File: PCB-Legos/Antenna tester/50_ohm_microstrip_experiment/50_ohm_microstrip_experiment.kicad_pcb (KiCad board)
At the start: 4 copper layers, 45.7 x 66.5 mm, 9 parts, among them J1 Conn_Coaxial, J3 Conn_Coaxial, J4 Conn_Coaxial, J5 Conn_Coaxial

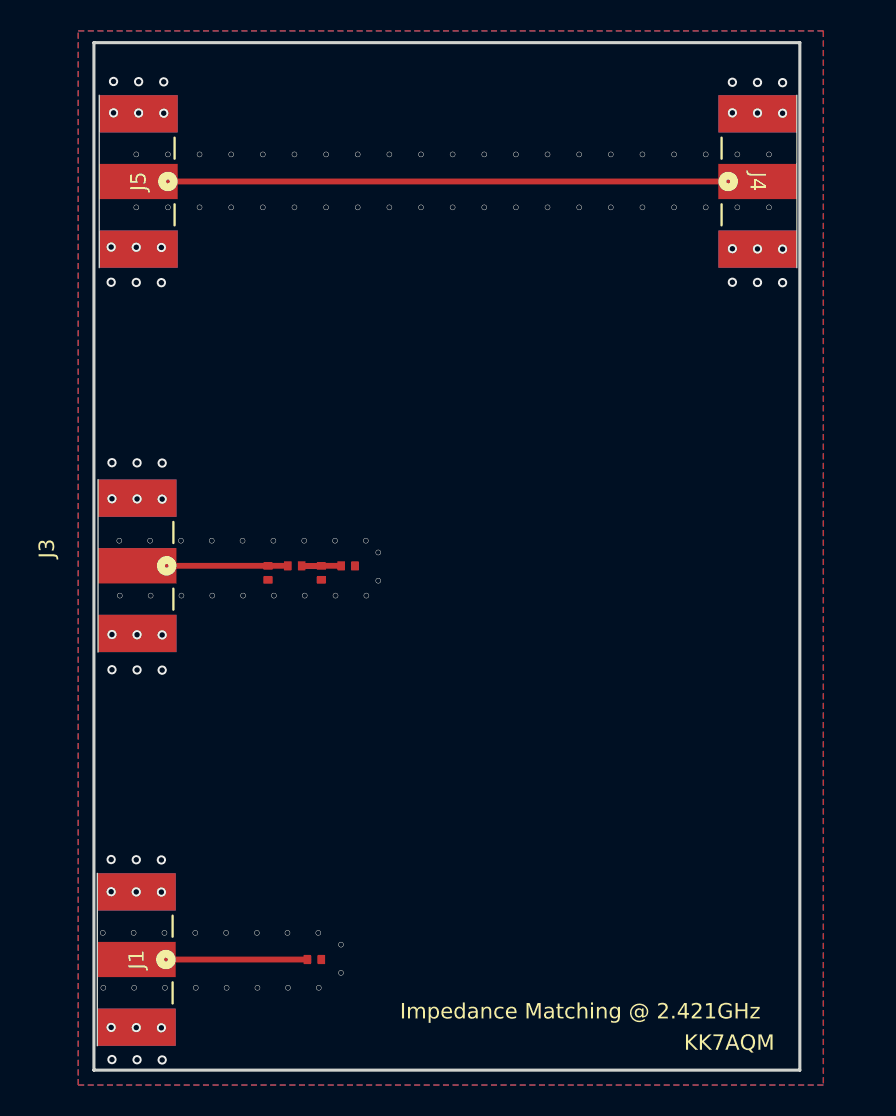
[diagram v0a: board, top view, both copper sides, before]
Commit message: Update with open stub/ changes
-Added vias, removed DNP components, moved components closer together
- implemented open stub experiment
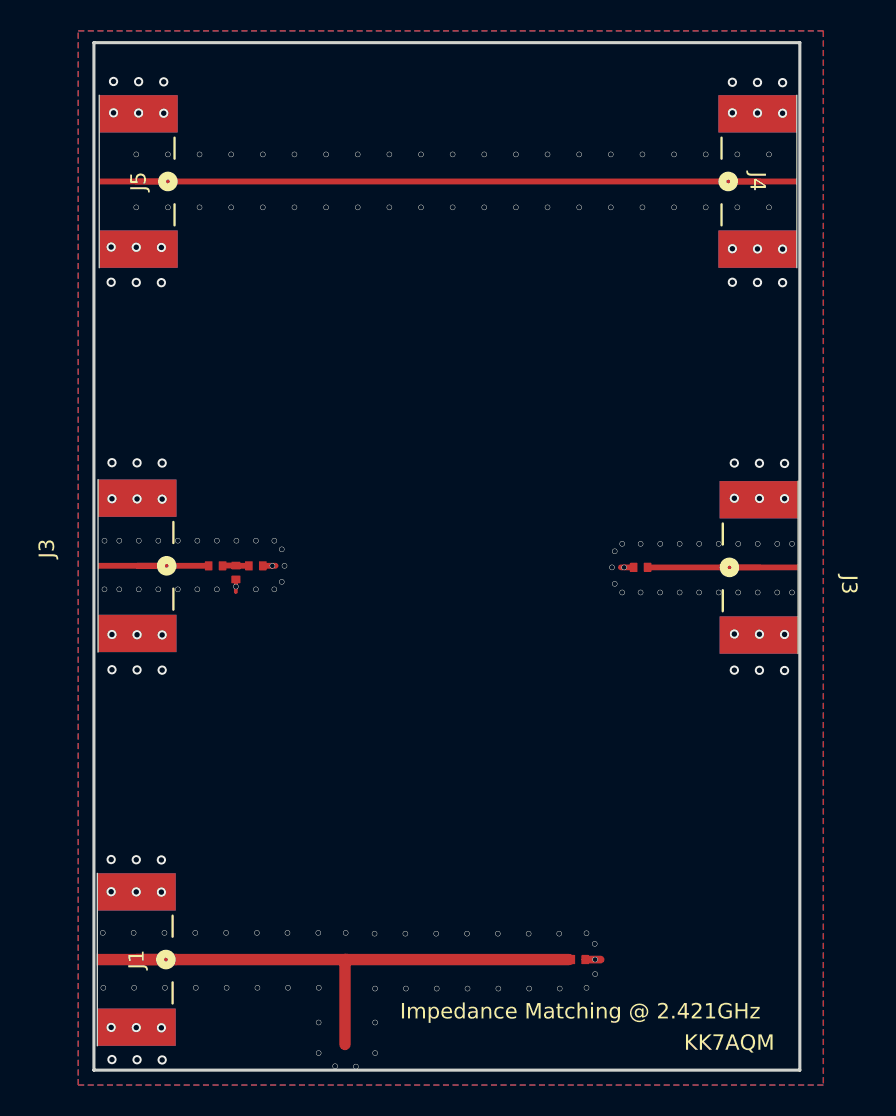
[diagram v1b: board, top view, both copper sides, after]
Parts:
- removed R4: 0, HGS_Reflector:.0402-C-NOSILK
- added J3: Conn_Coaxial, Cinch:CONN_142-0701-851_CIN, F.Cu at (174.3, 64.2)
- added R5: 0, HGS_Reflector:.0402-C-NOSILK, F.Cu at (166.5, 64.2)
- R1: value 50 -> 150
- moved R1 17.1 mm to (162.4, 89.6)
- moved R5 5.97 mm to (141.6, 64.1)
- moved R2 5.54 mm to (140.3, 64.5)
- moved R3 5.12 mm to (138.9, 64.1)
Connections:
- J1 pad 4: GND -> (no net)
- J1 pad 5: GND -> (no net)
- J3 pad 4: GND -> (no net)
- J3 pad 5: GND -> (no net)
- J4 pad 4: GND -> (no net)
- J4 pad 5: GND -> (no net)
- J5 pad 4: GND -> (no net)
- J5 pad 5: GND -> (no net)
- R1 pad 1: GND -> Net-(J1-Pad1)
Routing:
- net Net-(J1-Pad1): track 11.3 -> 34.7 mm
- net GND: track 0.00 -> 2.53 mm, vias 128 -> 192
- net Net-(J3-Pad1): track 9.75 -> 11.9 mm
- net Net-(R2-Pad2): track 2.63 -> 1.82 mm

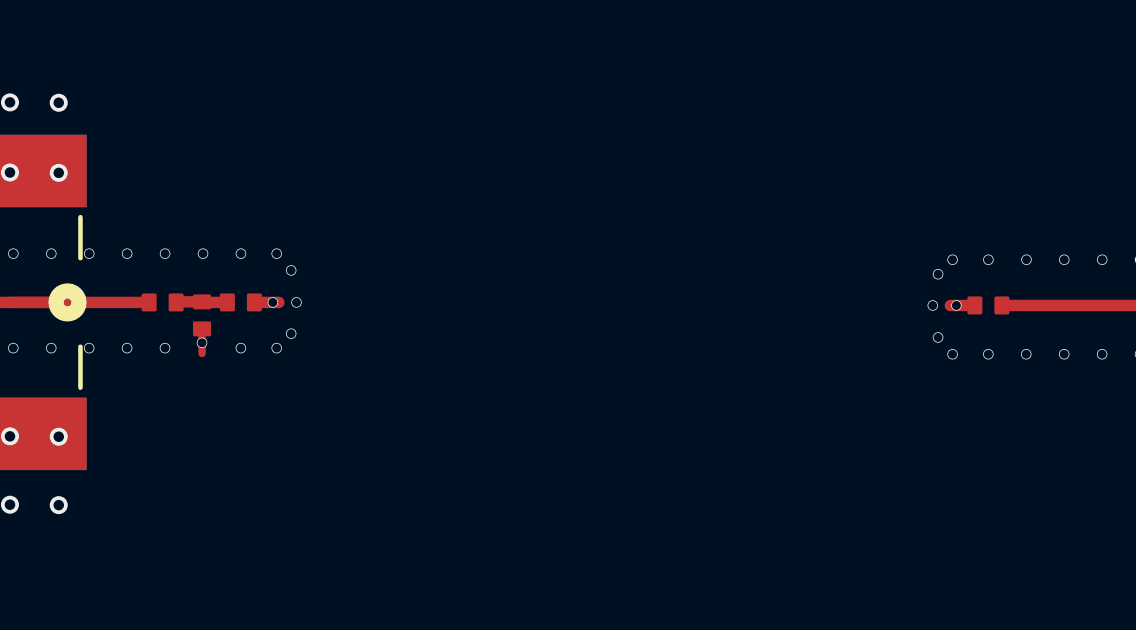
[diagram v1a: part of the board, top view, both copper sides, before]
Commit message: Matching Board with open stub
Added extra vias around pads
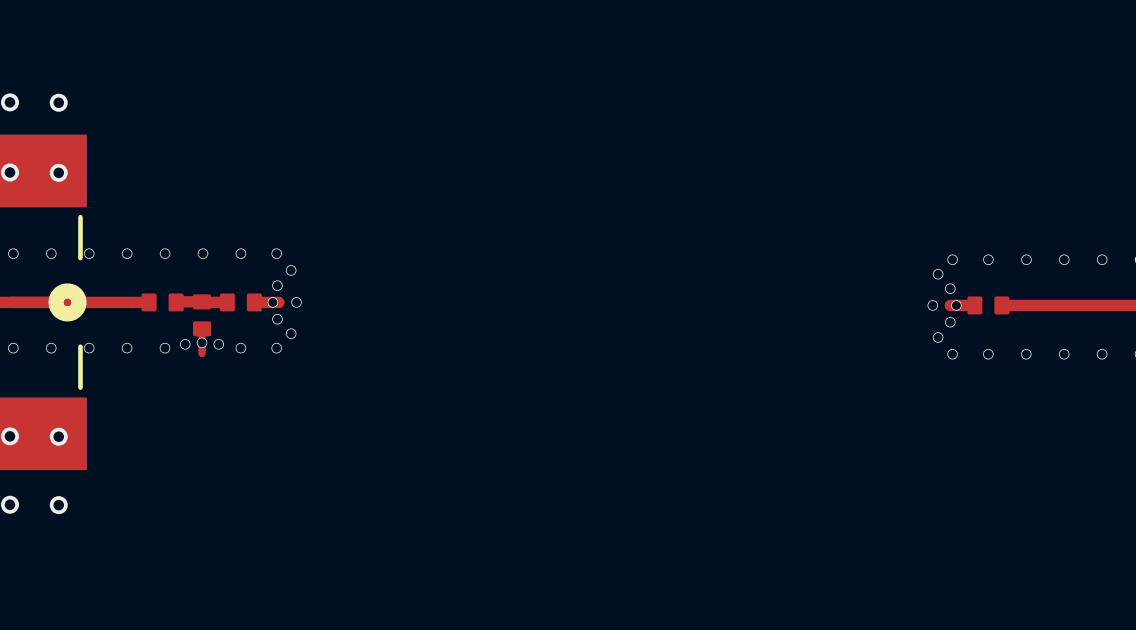
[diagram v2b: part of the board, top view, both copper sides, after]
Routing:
- net GND: vias 192 -> 198
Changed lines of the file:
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@@
   (via (at 161.23285 91.4908) (size 0.35) (drill 0.3) (layers "F.Cu" "B.Cu") (free) (net 1))
   (via (at 166.469486 65.8368) (size 0.35) (drill 0.3) (layers "F.Cu" "B.Cu") (free) (net 1))
+  (via (at 165.2016 63.6524) (size 0.35) (drill 0.3) (layers "F.Cu" "B.Cu") (free) (net 1))
   (via (at 172.736927 40.894) (size 0.35) (drill 0.3) (layers "F.Cu" "B.Cu") (free) (net 1))
   (via (at 135.4328 43.49115) (size 0.6) (drill 0.35) (layers "F.Cu" "B.Cu") (free) (net 1))
@@
   (via (at 166.590128 37.465) (size 0.35) (drill 0.3) (layers "F.Cu" "B.Cu") (free) (net 1))
   (via (at 148.149731 37.465) (size 0.35) (drill 0.3) (layers "F.Cu" "B.Cu") (free) (net 1))
+  (via (at 165.2016 64.77) (size 0.35) (drill 0.3) (layers "F.Cu" "B.Cu") (free) (net 1))
   (via (at 132.2324 96.0882) (size 0.6) (drill 0.35) (layers "F.Cu" "B.Cu") (free) (net 1))
   (via (at 174.1678 57.4675) (size 0.6) (drill 0.35) (layers "F.Cu" "B.Cu") (free) (net 1))
@@
   (via (at 133.8072 83.1469) (size 0.6) (drill 0.35) (layers "F.Cu" "B.Cu") (free) (net 1))
   (via (at 175.7934 57.4802) (size 0.6) (drill 0.35) (layers "F.Cu" "B.Cu") (free) (net 1))
+  (via (at 140.8176 65.5066) (size 0.35) (drill 0.3) (layers "F.Cu" "B.Cu") (free) (net 1))
   (via (at 167.733742 65.8368) (size 0.35) (drill 0.3) (layers "F.Cu" "B.Cu") (free) (net 1))
+  (via (at 139.7 65.5066) (size 0.35) (drill 0.3) (layers "F.Cu" "B.Cu") (free) (net 1))
   (via (at 162.9664 91.44) (size 0.35) (drill 0.3) (layers "F.Cu" "B.Cu") (free) (net 1))
   (via (at 135.4836 59.7916) (size 0.6) (drill 0.35) (layers "F.Cu" "B.Cu") (free) (net 1))
@@
   (via (at 133.858 96.1009) (size 0.6) (drill 0.35) (layers "F.Cu" "B.Cu") (free) (net 1))
   (via (at 132.1816 43.46575) (size 0.6) (drill 0.35) (layers "F.Cu" "B.Cu") (free) (net 1))
+  (via (at 142.7734 64.6684) (size 0.35) (drill 0.3) (layers "F.Cu" "B.Cu") (free) (net 1))
   (via (at 139.657664 91.44) (size 0.35) (drill 0.3) (layers "F.Cu" "B.Cu") (free) (net 1))
   (via (at 135.5852 34.798) (size 0.6) (drill 0.35) (layers "F.Cu" "B.Cu") (free) (net 1))
@@
   (via (at 137.627782 87.884) (size 0.35) (drill 0.3) (layers "F.Cu" "B.Cu") (free) (net 1))
   (via (at 142.748 62.484) (size 0.35) (drill 0.3) (layers "F.Cu" "B.Cu") (free) (net 1))
+  (via (at 142.7734 63.5508) (size 0.35) (drill 0.3) (layers "F.Cu" "B.Cu") (free) (net 1))
   (via (at 135.856133 40.894) (size 0.35) (drill 0.3) (layers "F.Cu" "B.Cu") (free) (net 1))
   (via (at 175.7934 68.5546) (size 0.6) (drill 0.35) (layers "F.Cu" "B.Cu") (free) (net 1))

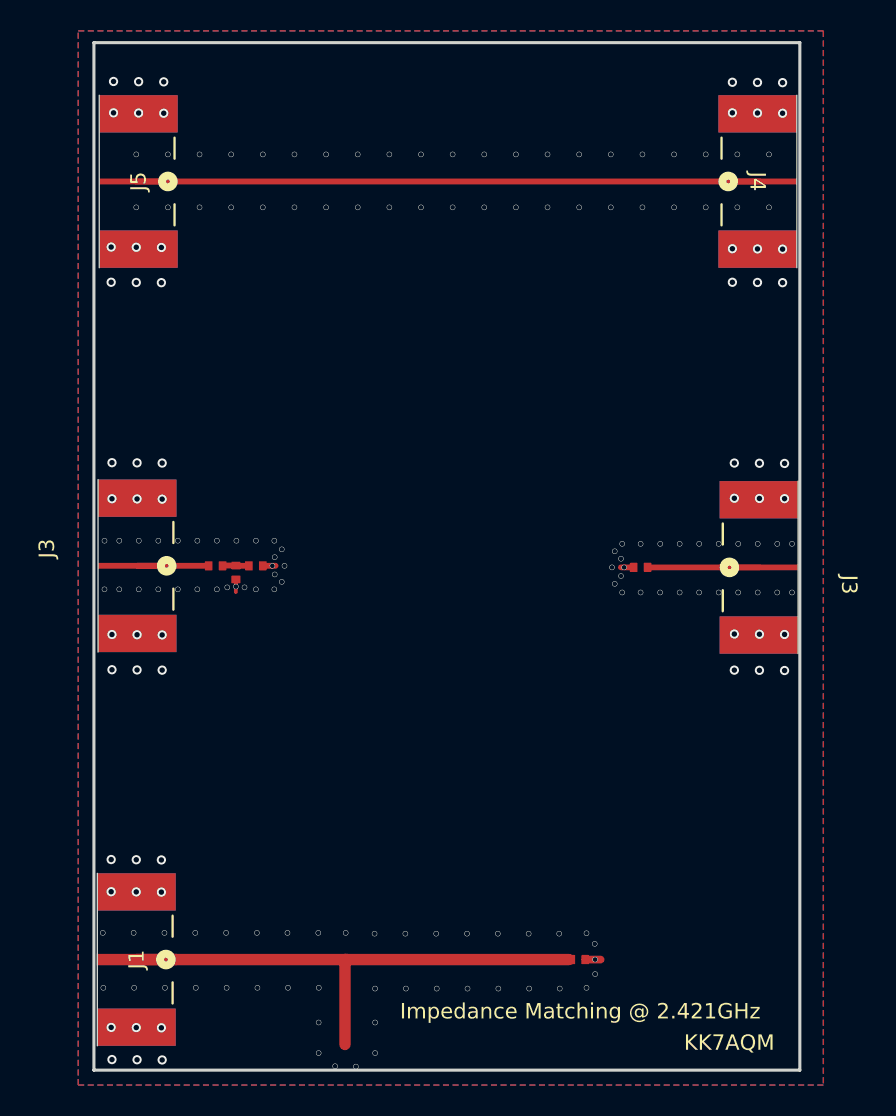
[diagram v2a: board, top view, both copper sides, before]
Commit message: Fixed vias and ground plane
moved some vias around and fixed the ground plane around the stub to follow the 3W rule.
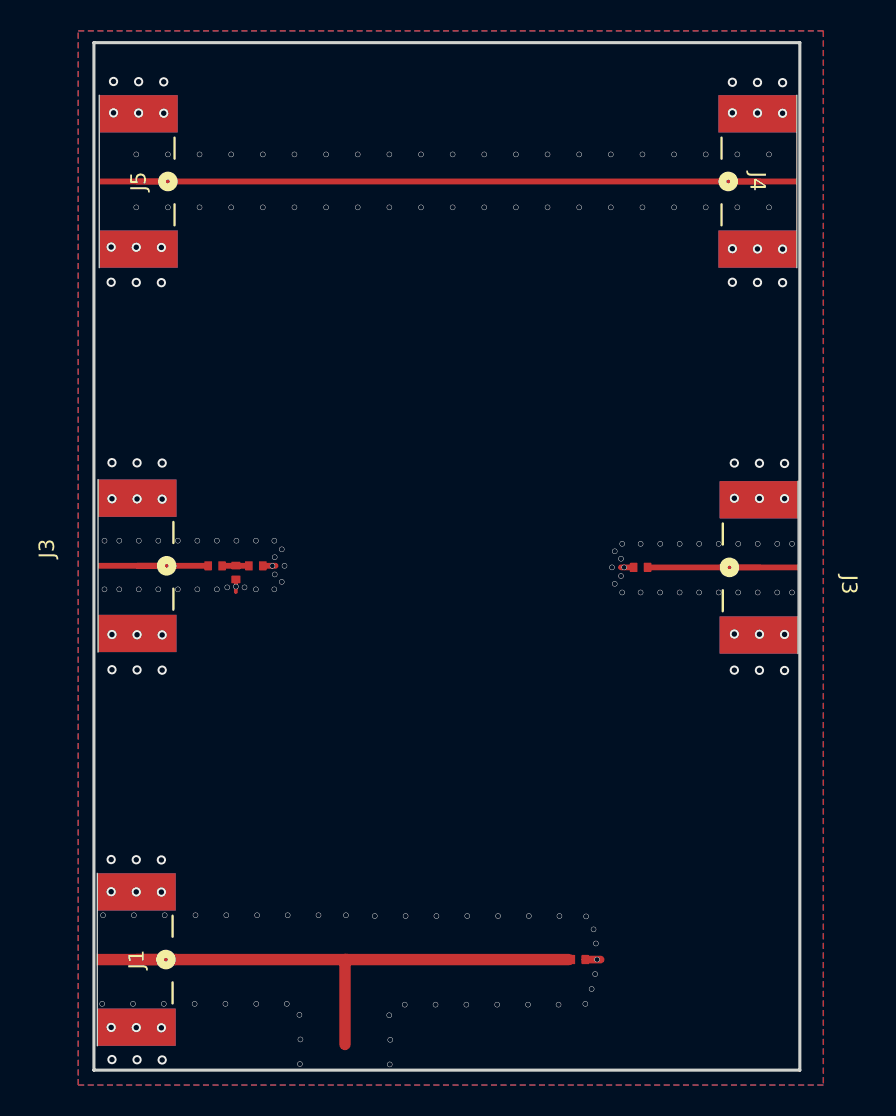
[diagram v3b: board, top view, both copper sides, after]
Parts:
- removed R2, R3: 0, HGS_Reflector:.0402-C-NOSILK
- added C1: .9pF, HGS_Reflector:.0402-C-NOSILK, F.Cu at (138.9, 64.1)
- added L1: 7nH, HGS_Reflector:.0402-C-NOSILK, F.Cu at (140.3, 64.5)
- R1: value 150 -> 50
- R5 (x2): value 0 -> 150
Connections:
- J1 pad 3: GND -> (no net)
- J3 pad 3: GND -> (no net) (x2)
- J4 pad 3: GND -> (no net)
- J5 pad 3: GND -> (no net)
- R1 pad 1: Net-(J1-Pad1) -> GND
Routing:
- net Net-(R5-Pad2): track 1.82 -> 9.68 mm
- net Net-(J3-Pad1): track 11.9 -> 4.64 mm
- net Net-(J1-Pad1): track 34.7 -> 33.7 mm
- net GND: track 2.53 -> 3.53 mm
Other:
- board text removed: "Impedance Matching @ 2.421GHz"
- board text removed: "KK7AQM"
